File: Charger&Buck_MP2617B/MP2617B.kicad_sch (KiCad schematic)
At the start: 41 parts, among them J2 Jumper

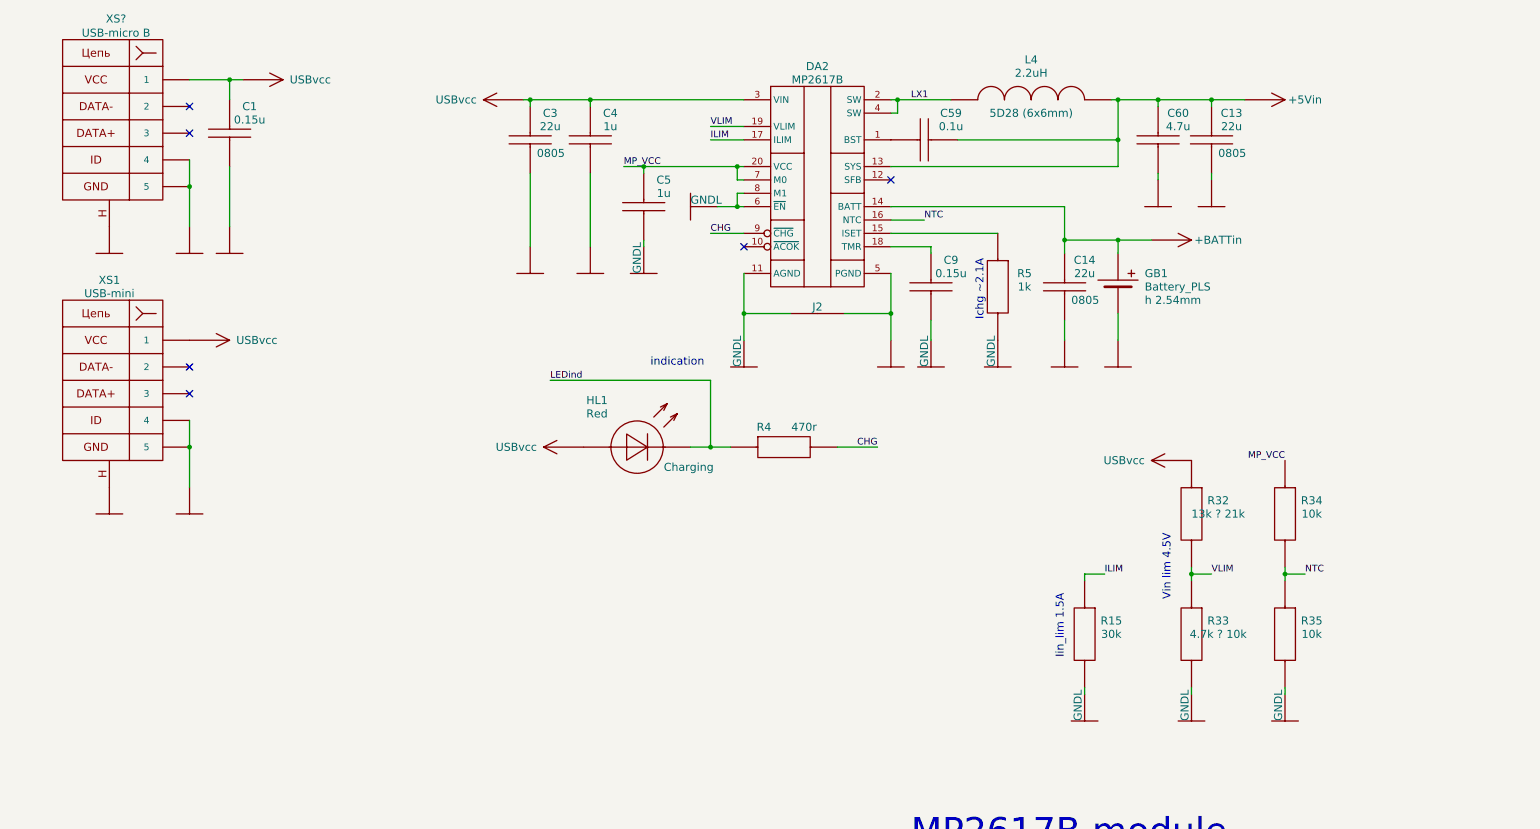
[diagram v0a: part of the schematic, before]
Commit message: добавлена цепь Vsys_FB
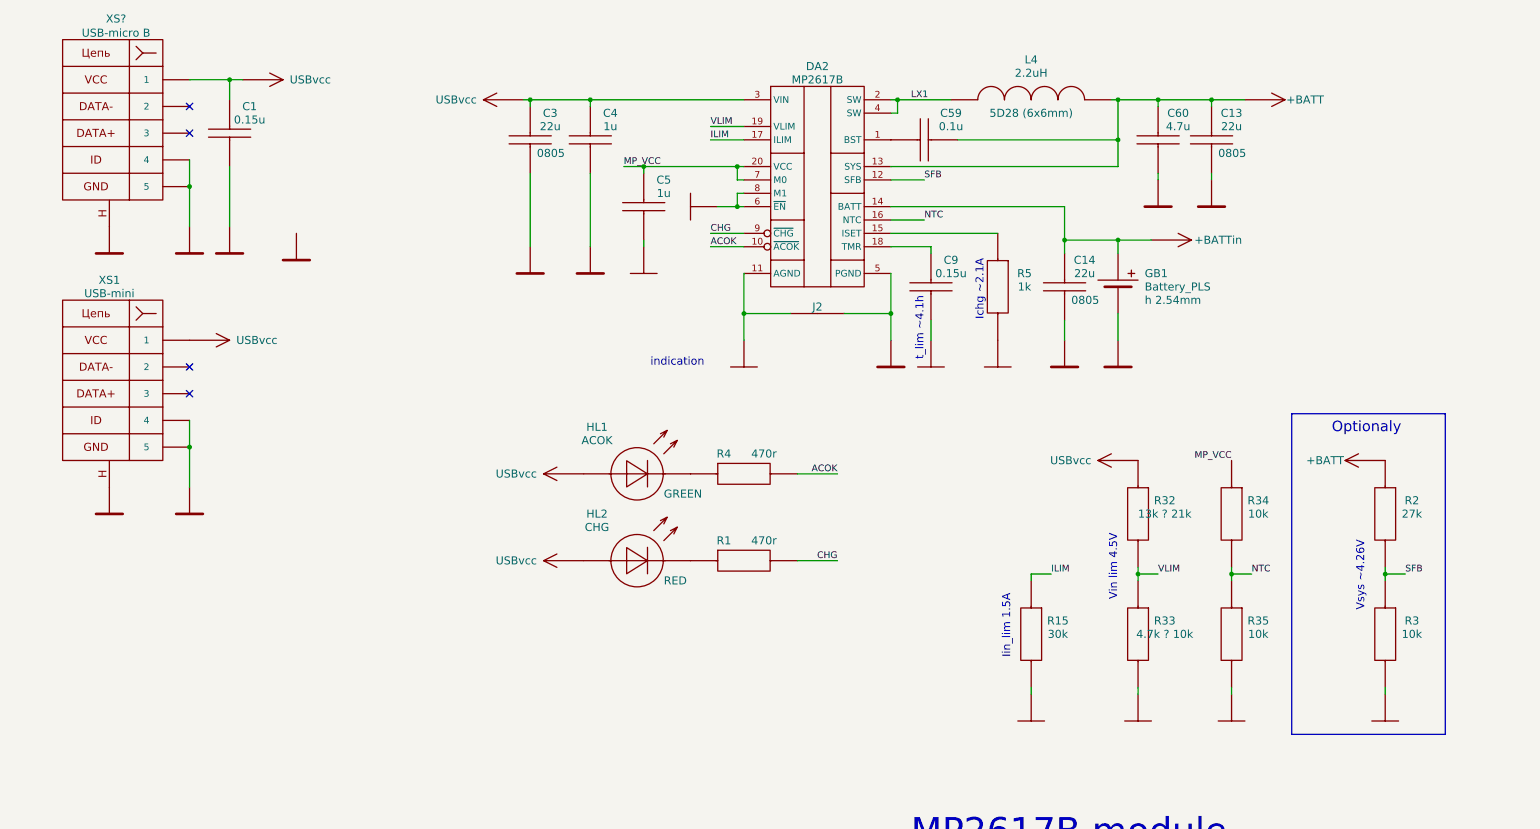
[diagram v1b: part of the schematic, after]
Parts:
- added HL2: CHG, LEDs:LED0805, symbol LED:LED_0805
- added R1: 470r, Resistors:RES0603, symbol Resistors:R_0603
- added R2: 27k, Resistors:RES0603, symbol Resistors:R_0603
- added R3: 10k, Resistors:RES0603, symbol Resistors:R_0603
- HL1: value Red -> ACOK; Comment Charging -> GREEN
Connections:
- net GNDL is gone; now on net GND: C5.2, C9.2, DA2.11 (AGND), DA2.6 (~{EN}), DA2.8 (M1), J2.1
- net CHG: now also R1.2; no longer R4.2
- net GND: no longer C1.2, C13.2, C14.2, C3.2, C4.2, C60.2, DA2.5 (PGND), GB1.2 (-), J2.2, XS1.4, XS1.5, XS1.SHLD, XS?.4, XS?.5, XS?.SHLD
- net ACOK: now reaches DA2.10 (~{ACOK})
- net ACOK: now also R4.2
- net SFB: now reaches DA2.12 (SFB)
- net +5Vin renamed +BATT
- net LEDind: no longer names the net of R4.1
- new net GNDP: C1.2, C13.2, C14.2, C3.2, C4.2, C60.2, DA2.5 (PGND), GB1.2 (-), J2.2, XS1.4, XS1.5, XS1.SHLD, XS?.4, XS?.5, XS?.SHLD
- no-connect marks 8 -> 6
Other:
- note added: "Optionaly"
- note added: "Vsys ~4.26V"
- note added: "t_lim ~4.1h"
- moved on the sheet: HL1, R15, R32, R33, R34, R35, R4

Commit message: Основная схема завершена
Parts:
- removed C11: 22u, Capacitors:CAP0603, symbol Capacitors:C_0603
- removed C12: 47u, Capacitors:CAP1206, symbol Capacitors:C_1206
- removed C21: 150p, Capacitors:CAP0603, symbol Capacitors:C_0603
- removed DA2: MP2637, QFN,_DFN,_LGA:FCQFN24, symbol Chargers:MP2637
- removed R10: 4.7k, Resistors:RES0603, symbol Resistors:R_0603
- removed R13: 22k, Resistors:RES0603, symbol Resistors:R_0603
- removed R14: 5.1k, Resistors:RES0603, symbol Resistors:R_0603
- removed R16, R17, R8: 10k, Resistors:RES0603, symbol Resistors:R_0603
- removed R18: 30k, Resistors:RES0603, symbol Resistors:R_0603
- removed R19: 12k, Resistors:RES0603, symbol Resistors:R_0603
- removed R20: 51k, Resistors:RES0603, symbol Resistors:R_0603
- removed R6: 0.02r, Resistors:RES0805, symbol Resistors:R_0805
- removed R9: 13k, Resistors:RES0603, symbol Resistors:R_0603
- L4: Size 5D28 (6x6mm) -> 5D28, NR6020 (6x6mm)
- R32: value 13k ? 21k -> 10k
- R33: value 4.7k ? 10k -> 16k
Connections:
- no-connect marks 6 -> 4
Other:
- note added: "Vin lim 3.95V"
- note added: "Vsys 4.26V"
- note removed: "Iout_lim 2.35A"
- note removed: "Vin 4.2~6.1V"
- note removed: "Vin lim 4.5V"
- note removed: "Vsys = 4.2V R22 27k, R23 6.8k for 6V"
- note removed: "Vsys ~4.26V"
- note removed: "configuration"
- moved on the sheet: C13, C60, L4

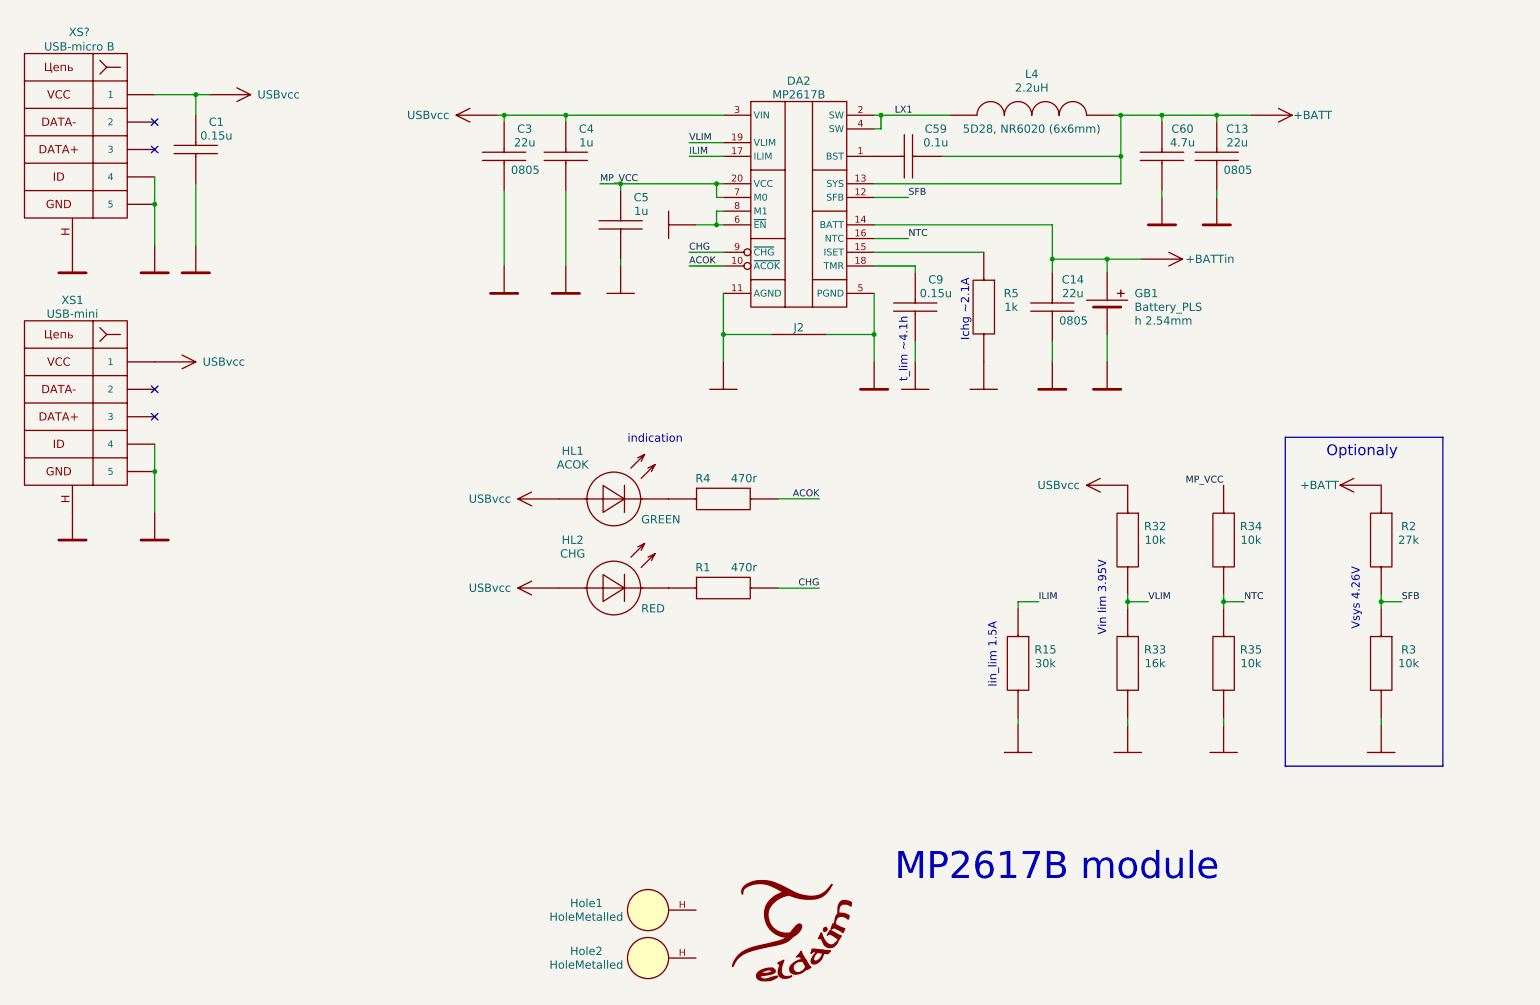
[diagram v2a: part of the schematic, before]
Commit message: +USB type-C & Power Delivery
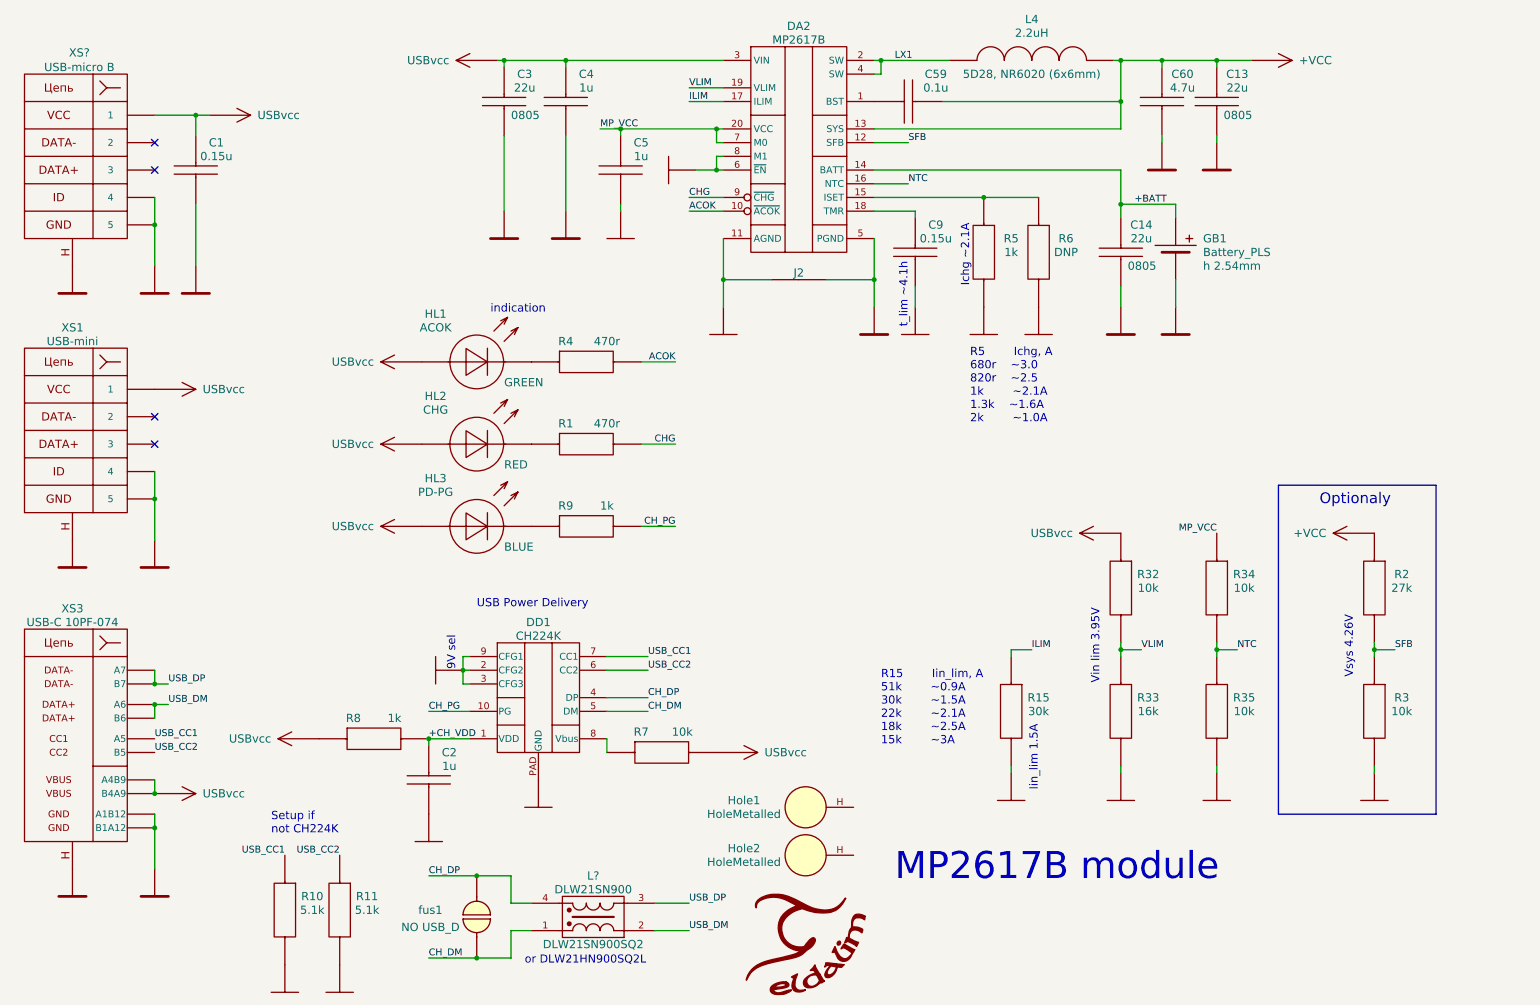
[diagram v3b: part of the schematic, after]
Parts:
- added C2: 1u, Capacitors:CAP0603, symbol Capacitors:C_0603
- added DD1: CH224K, HTSSOP-10, symbol Interface:CH224K
- added HL3: PD-PG, LEDs:LED0805, symbol LED:LED_0805
- added L?: DLW21SN900, Inductors:Choke_0805, symbol Protection:DLW21SN900
- added R10, R11: 5.1k, Resistors:RES0603, symbol Resistors:R_0603
- added R6: DNP, Resistors:RES0603, symbol Resistors:R_0603
- added R7: 10k, Resistors:RES0603, symbol Resistors:R_0603
- added R8, R9: 1k, Resistors:RES0603, symbol Resistors:R_0603
- added XS3: USB-C 10PF-074, symbol Connectors:USB-C_16pin
- added fus1: NO USB_D, FuseSolder, symbol PCB_details:Fuse
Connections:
- net +BATTin is gone; now on net +BATT: C14.1, DA2.14 (BATT), GB1.1 (+)
- net +BATT: no longer C13.1, C60.1, DA2.13 (SYS), L4.2
- net +USBvcc: now also R7.2, R8.1, XS3.A4B9, XS3.B4A9
- net GND: now also C2.2, DD1.2 (CFG2), DD1.3 (CFG3), DD1.9 (CFG1), DD1.PAD (GND)
- net GNDP: now also XS3.A1B12, XS3.B1A12, XS3.SHLD
- new net: DD1.8 (Vbus), R7.1
- new net +CH_VDD: C2.1, DD1.1 (VDD), R8.2
- new net +VCC: C13.1, C60.1, DA2.13 (SYS), L4.2
- new net CH_DM: DD1.5 (DM), L?.1, fus1.1
- new net CH_DP: DD1.4 (DP), L?.4, fus1.2
- new net CH_PG: DD1.10 (PG), R9.2
- new net USB_CC1: DD1.7 (CC1), XS3.A5
- new net USB_CC2: DD1.6 (CC2), XS3.B5
- new net USB_DM: L?.2, XS3.A6, XS3.B6
- new net USB_DP: L?.3, XS3.A7, XS3.B7
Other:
- note added: "9V sel"
- note added: "R15 Iin_lim, A 51k ~0.9A 30k ~1.5A 22k ~2.1A 18k ~2.5A 15k ~3A"
- note added: "R5 Ichg, A 680r ~3.0 820r ~2.5 1k ~2.1A 1.3k ~1.6A 2k ~1.0A"
- note added: "Setup if not CH224K"
- note added: "USB Power Delivery"
- note added: "or DLW21HN900SQ2L"
- moved on the sheet: C1, C13, C14, C3, C4, C5, C59, C60, C9, DA2, GB1, HL1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

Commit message: компоненты расставлены
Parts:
- removed XS1: USB-mini, USB-mini_B, symbol Connectors:USB-mini
- added XP1: +Vin, Connectors:PLS-1, symbol Connectors:Conn-1m
- added XP2: GND, Connectors:PLS-1Rnd, symbol Connectors:Conn-1m
- C1: value 0.15u -> 0.1u
- DA1: renamed from DA2; footprint FCQFN20 -> QFN,_DFN,_LGA:FCQFN20
- DD1: footprint HTSSOP-10 -> SOP,_MSOP,_TSSOP:HESOP10
- Hole?: renamed from Hole2; symbol MP2637-rescue:HoleMetalled -> PCB_details:HoleMetalled
- Hole?: renamed from Hole1; symbol MP2637-rescue:HoleMetalled -> PCB_details:HoleMetalled
- J1: renamed from J2; footprint (none) -> PCB_details:Jump_0.5mm
- Logo1: footprint Graphics:Eldalim_15x12 -> Graphics:Eldalim_12x10
- R6: renamed from R9; value 1k -> 470r
- XS1: renamed from XS3; value USB-C 10PF-074 -> USB-C 16PF-015; footprint (none) -> Connectors:USB-C_16pin_16PF-015
- fus1: footprint FuseSolder -> PCB_details:FuseSolder
- renumbered C13 to C10, C59 to C6, C9 to C7, C14 to C8, C60 to C9, L4 to L2, R10 to R1, R6 to R10, R32 to R11, R33 to R12, R34 to R13, R35 to R14, R2 to R15, R3 to R16, R11 to R2, R8 to R3, R1 to R5, R5 to R8, R15 to R9
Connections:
- net +USBvcc: now also XP1.1
- net CH_DM: now also fus1.2; no longer fus1.1
- net CH_DP: now also fus1.1; no longer fus1.2
- net GND: no longer C2.2, DD1.2 (CFG2), DD1.3 (CFG3), DD1.9 (CFG1), DD1.PAD (GND)
- net GNDP: now also C2.2, DD1.2 (CFG2), DD1.3 (CFG3), DD1.9 (CFG1), DD1.PAD (GND), Hole?.H, Hole?.H, XP2.1
- net USB_DM: now also XS1.A7, XS1.B7; no longer XS1.A6, XS1.B6
- net USB_DP: now also XS1.A6, XS1.B6; no longer XS1.A7, XS1.B7
- no-connect marks 4 -> 2
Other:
- moved on the sheet: C2, DD1, Hole?, L?, R1, R2, R3, R7, XS1, fus1

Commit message: трассирровка завершкна, шелкография сделана.
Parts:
- GB1: value Battery_PLS -> Battery
- XS1: value USB-C 16PF-015 -> USBC 16PF-015
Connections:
- net GND: now also C1.2, C10.2, C2.2, C3.2, C4.2, C8.2, C9.2, DA1.5 (PGND), DD1.PAD (GND), GB1.2 (-), Hole?.H, Hole?.H, J1.2, XP2.1, XS1.A1B12, XS1.B1A12, XS1.SHLD, XS?.4, XS?.5, XS?.SHLD; no longer C5.2, C7.2, DA1.11 (AGND), DA1.6 (~{EN}), DA1.8 (M1), J1.1
- net GNDP: no longer C1.2, C10.2, C2.2, C3.2, C4.2, C8.2, C9.2, DA1.5 (PGND), DD1.PAD (GND), GB1.2 (-), Hole?.H, Hole?.H, J1.2, XP2.1, XS1.A1B12, XS1.B1A12, XS1.SHLD, XS?.4, XS?.5, XS?.SHLD
- net MP_VCC: no longer C5.1, DA1.20 (VCC), DA1.7 (M0)
- net LX1 renamed +LX1
- new net +MP_VCC: C5.1, DA1.20 (VCC), DA1.7 (M0)
- new net GNDL: C5.2, C7.2, DA1.11 (AGND), DA1.6 (~{EN}), DA1.8 (M1), J1.1
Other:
- note added: "R8 Ichg, A 680r ~3.0 820r ~2.5 1k ~2.1A 1.3k ~1.6A 2k ~1.0A"
- note added: "R9 Iin_lim, A 51k ~0.9A 30k ~1.5A 22k ~2.1A 18k ~2.5A 15k ~3A"
- note removed: "R15 Iin_lim, A 51k ~0.9A 30k ~1.5A 22k ~2.1A 18k ~2.5A 15k ~3A"
- note removed: "R5 Ichg, A 680r ~3.0 820r ~2.5 1k ~2.1A 1.3k ~1.6A 2k ~1.0A"

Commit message: исправления и дополнения
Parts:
- C3: value 22u -> 22u 16V
- C4: value 1u -> 1u 16V
- L?: now not fitted
- R11: value 10k -> 16k
- R12: value 16k -> 10k
- R4, R5, R6: value 470r -> 1k
- R9: value 30k -> 22k
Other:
- note added: "M1 M0 0 0 - USB2 (Iin lim 450mA) 0 1 - Prog (R i_lim set) 1 0 - USB3 (Iin lim 825mA) 1 1 - DEF (Iin lim 2A) "0" < 0.4V "1" > 1.5V"
- note added: "R9 Iin_lim, A 51k ~0.9A 30k ~1.5A 22k ~2.1A"
- note added: "Vsel R 5V -> 470r 9V -> 1k"
- note removed: "Iin_lim 1.5A"
- note removed: "R9 Iin_lim, A 51k ~0.9A 30k ~1.5A 22k ~2.1A 18k ~2.5A 15k ~3A"
- moved on the sheet: C3, L2
